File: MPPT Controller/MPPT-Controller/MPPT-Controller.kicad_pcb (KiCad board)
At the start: 4 copper layers, 79 parts, among them J1 Conn_01x02_Pin, J2 Conn_01x02_Pin, J3 Conn_01x02_Pin, J4 Conn_01x02_Pin, J5 USB_C_Receptacle_USB2.0_16P, J6 Conn_01x02_Pin, Q1 IRL540N, SW1 SW_SPDT, U1 ADS1115IDGS, U2 ESP32-WROOM-32D, U3 CH340C, U4 LM1117DT-3.3, U5 LM2596S-ADJ, U6 TC4422, U7 ADS1115IDGS

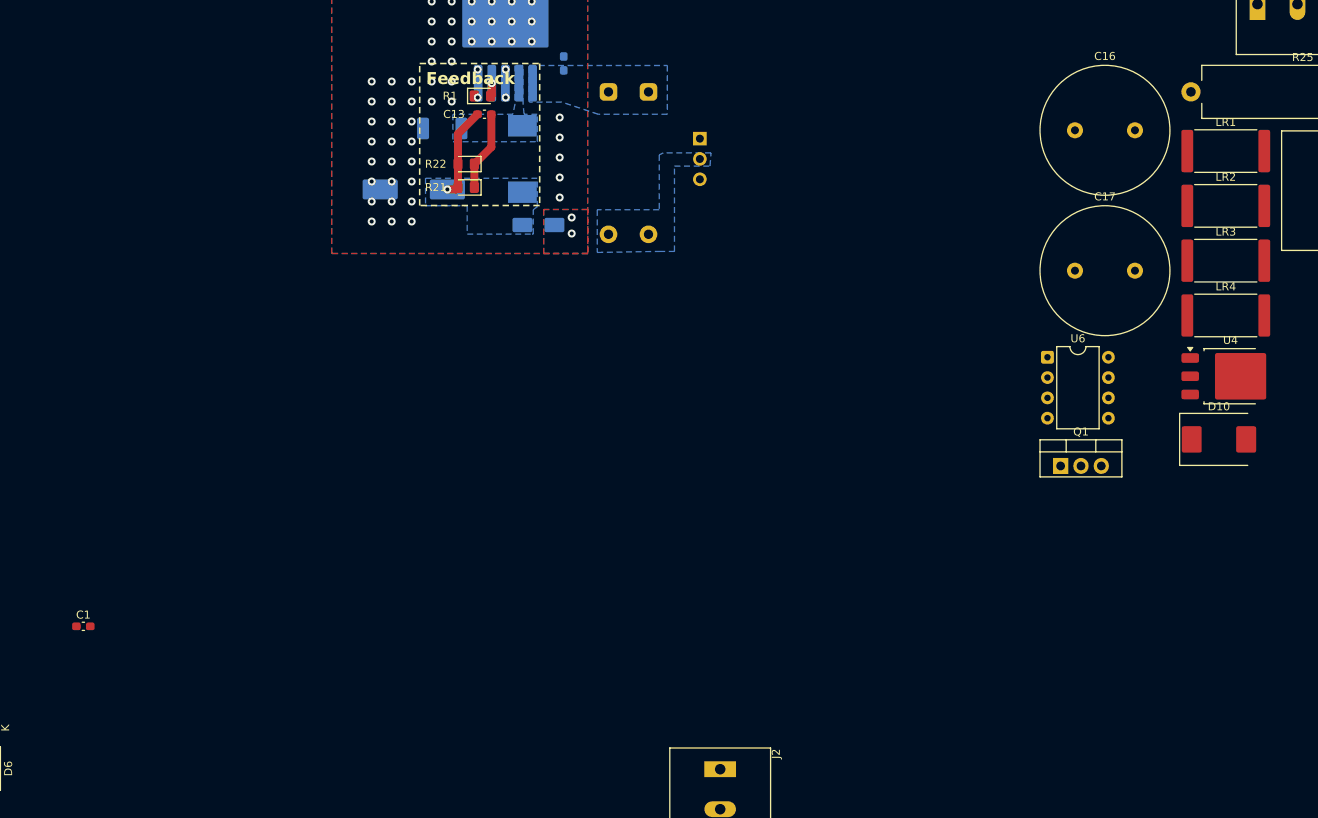
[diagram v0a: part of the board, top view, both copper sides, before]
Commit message: Move Shunts
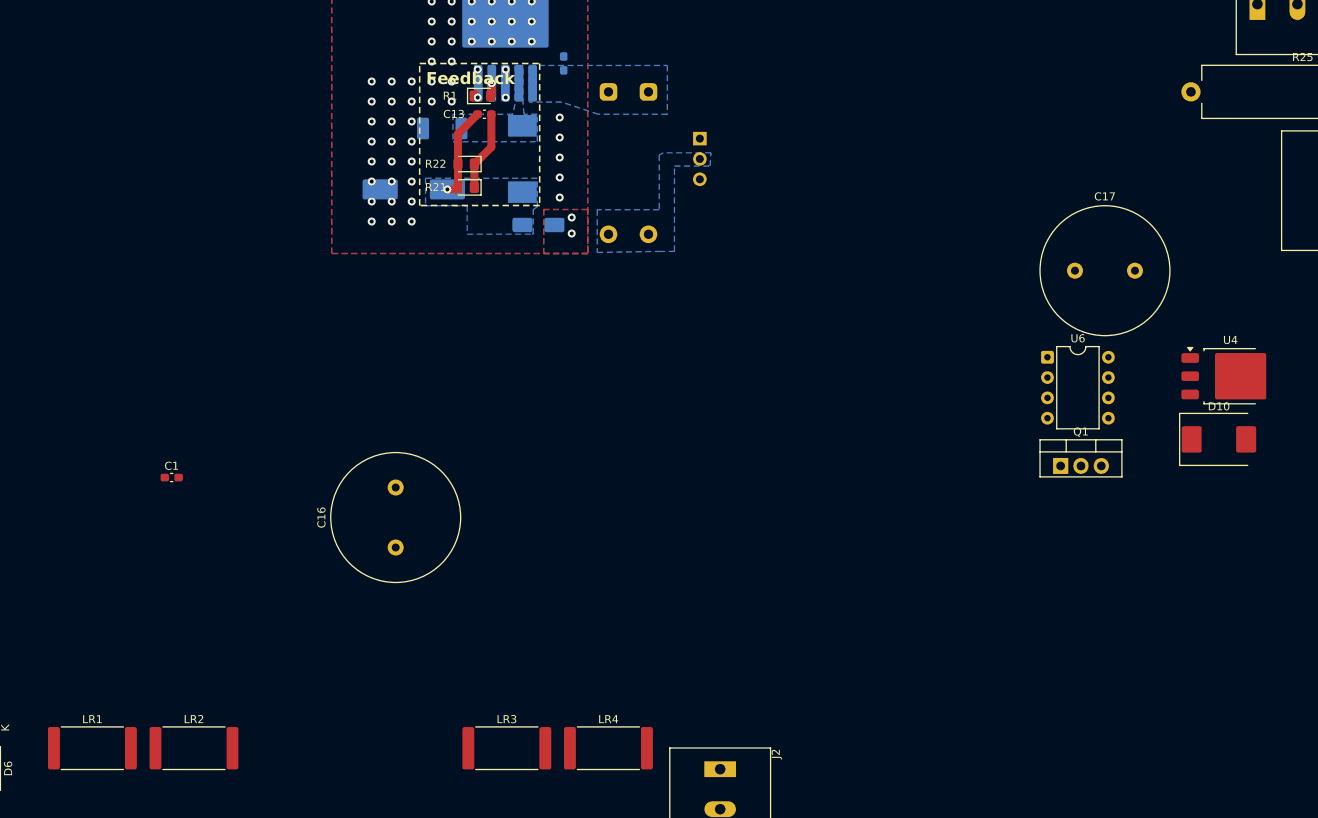
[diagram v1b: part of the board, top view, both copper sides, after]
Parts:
- moved LR1 160.1 mm to (84.1, 116.8)
- moved LR2 145.7 mm to (96.8, 116.8)
- moved LR3 108.6 mm to (135.9, 116.8)
- moved C16 99.6 mm to (122.0, 91.8), turned to 90 degrees
- moved LR4 94.2 mm to (148.6, 116.8)
- moved C1 21.6 mm to (94.0, 83.0)
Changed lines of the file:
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@@
 	(footprint "Capacitor_THT:C_Radial_D16.0mm_H25.0mm_P7.50mm"
 		(layer "F.Cu")
-		(at 206.91 39.595)
+		(at 122 91.75 90)
 		(descr "C, Radial series, Radial, pin pitch=7.50mm, diameter=16mm, height=25mm, Non-Polar Electrolytic Capacitor")
 		(tags "C Radial series Radial pin pitch 7.50mm diameter 16mm height 25mm Non-Polar Electrolytic Capacitor")
 		(property "Reference" "C16"
-			(at 3.75 -9.25 0)
+			(at 3.75 -9.25 90)
 			(layer "F.SilkS")
 			(effects
@@
 		)
 		(property "Value" "470u"
-			(at 3.75 9.25 0)
+			(at 3.75 9.25 90)
 			(layer "F.Fab")
 			(effects
@@
 		)
 		(property "Datasheet" ""
-			(at 0 0 0)
+			(at 0 0 90)
 			(layer "F.Fab")
 			(hide yes)
@@
 		)
 		(property "Description" "Unpolarized capacitor"
-			(at 0 0 0)
+			(at 0 0 90)
 			(layer "F.Fab")
 			(hide yes)
@@
 		)
 		(fp_text user "${REFERENCE}"
-			(at 3.75 0 0)
+			(at 3.75 0 90)
 			(layer "F.Fab")
 			(effects
@@
 		)
 		(pad "1" thru_hole circle
-			(at 0 0)
+			(at 0 0 90)
 			(size 2 2)
 			(drill 1)
@@
 		)
 		(pad "2" thru_hole circle
-			(at 7.5 0)
+			(at 7.5 0 90)
 			(size 2 2)
 			(drill 1)
@@
 	(footprint "Resistor_SMD:R_4020_10251Metric"
 		(layer "F.Cu")
-		(at 225.76 55.895)
+		(at 135.89 116.84)
 		(descr "Resistor SMD 4020 (10251 Metric), square (rectangular) end terminal, IPC-7351 nominal, (Body size source: http://datasheet.octopart.com/HVC0603T5004FET-Ohmite-datasheet-26699797.pdf), generated with kicad-footprint-generator")
 		(tags "resistor")
@@
 	(footprint "Capacitor_SMD:C_0603_1608Metric_Pad1.08x0.95mm_HandSolder"
 		(layer "F.Cu")
-		(at 82.9575 101.6)
+		(at 94 83)
 		(descr "Capacitor SMD 0603 (1608 Metric), square (rectangular) end terminal, IPC-7351 nominal with elongated pad for handsoldering. (Body size source: IPC-SM-782 page 76, https://www.pcb-3d.com/wordpress/wp-content/uploads/ipc-sm-782a_amendment_1_and_2.pdf), generated with kicad-footprint-generator")
 		(tags "capacitor handsolder")
@@
 	(footprint "Resistor_SMD:R_4020_10251Metric"
 		(layer "F.Cu")
-		(at 225.76 49.045)
+		(at 96.7875 116.84)
 		(descr "Resistor SMD 4020 (10251 Metric), square (rectangular) end terminal, IPC-7351 nominal, (Body size source: http://datasheet.octopart.com/HVC0603T5004FET-Ohmite-datasheet-26699797.pdf), generated with kicad-footprint-generator")
 		(tags "resistor")
@@
 	(footprint "Resistor_SMD:R_4020_10251Metric"
 		(layer "F.Cu")
-		(at 225.76 62.745)
+		(at 148.59 116.84)
 		(descr "Resistor SMD 4020 (10251 Metric), square (rectangular) end terminal, IPC-7351 nominal, (Body size source: http://datasheet.octopart.com/HVC0603T5004FET-Ohmite-datasheet-26699797.pdf), generated with kicad-footprint-generator")
 		(tags "resistor")
@@
 	(footprint "Resistor_SMD:R_4020_10251Metric"
 		(layer "F.Cu")
-		(at 225.76 42.195)
+		(at 84.0875 116.84)
 		(descr "Resistor SMD 4020 (10251 Metric), square (rectangular) end terminal, IPC-7351 nominal, (Body size source: http://datasheet.octopart.com/HVC0603T5004FET-Ohmite-datasheet-26699797.pdf), generated with kicad-footprint-generator")
 		(tags "resistor")

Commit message: Compact
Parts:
- moved U2 254.5 mm to (45.9, 66.7)
- moved L2 154.9 mm to (92.7, 66.0), turned to 90 degrees
- moved C17 135.7 mm to (75.0, 88.9)
- moved U6 134.9 mm to (68.6, 66.0)
- moved Q1 109.9 mm to (95.6, 90.2), turned to -90 degrees
- moved C10 47.4 mm to (279.7, 32.0)
- moved C11 47.4 mm to (210.8, 78.2)
- moved C12 47.4 mm to (215.1, 63.1)
- moved C2 47.4 mm to (210.8, 65.6)
- moved C3 47.4 mm to (210.8, 68.1)
- moved C4 47.4 mm to (210.8, 70.7)
- moved C5 47.4 mm to (210.8, 73.2)
- moved C6 47.4 mm to (210.8, 75.7)
- moved C7 47.4 mm to (279.7, 24.4)
- moved C8 47.4 mm to (279.7, 26.9)
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
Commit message: Capacitors
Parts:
- C16, C17: moved to B.Cu
- moved Q1 22.3 mm to (74.5, 97.5), turned to 180 degrees
- moved C17 19.8 mm to (68.2, 107.5)
- moved C16 18.9 mm to (108.2, 107.5), turned to 180 degrees

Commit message: Layout
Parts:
- added HS1: Heatsink_Pad, Heatsink:Heatsink_AAVID_576802B03900G, B.Cu at (71.5, 92.0)
- added M1: Fan_4pin, Connector:FanPinHeader_1x04_P2.54mm_Vertical, F.Cu at (122.9, 81.0)
- Q1: moved to B.Cu
- moved L2 38.0 mm to (80.4, 102.0)
- moved U6 10.5 mm to (58.2, 64.2)
- moved C16 3.22 mm to (105.0, 107.5)
- moved J2 3.22 mm to (136.5, 105.5)
- moved LR3 3.22 mm to (109.8, 102.9)
- moved LR4 3.22 mm to (122.5, 102.9)
- moved Q1 1.11 mm to (73.5, 96.9)
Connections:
- R1 pad 1: GND -> Net-(U5-FB)
- R1 pad 2: Net-(U5-FB) -> GND

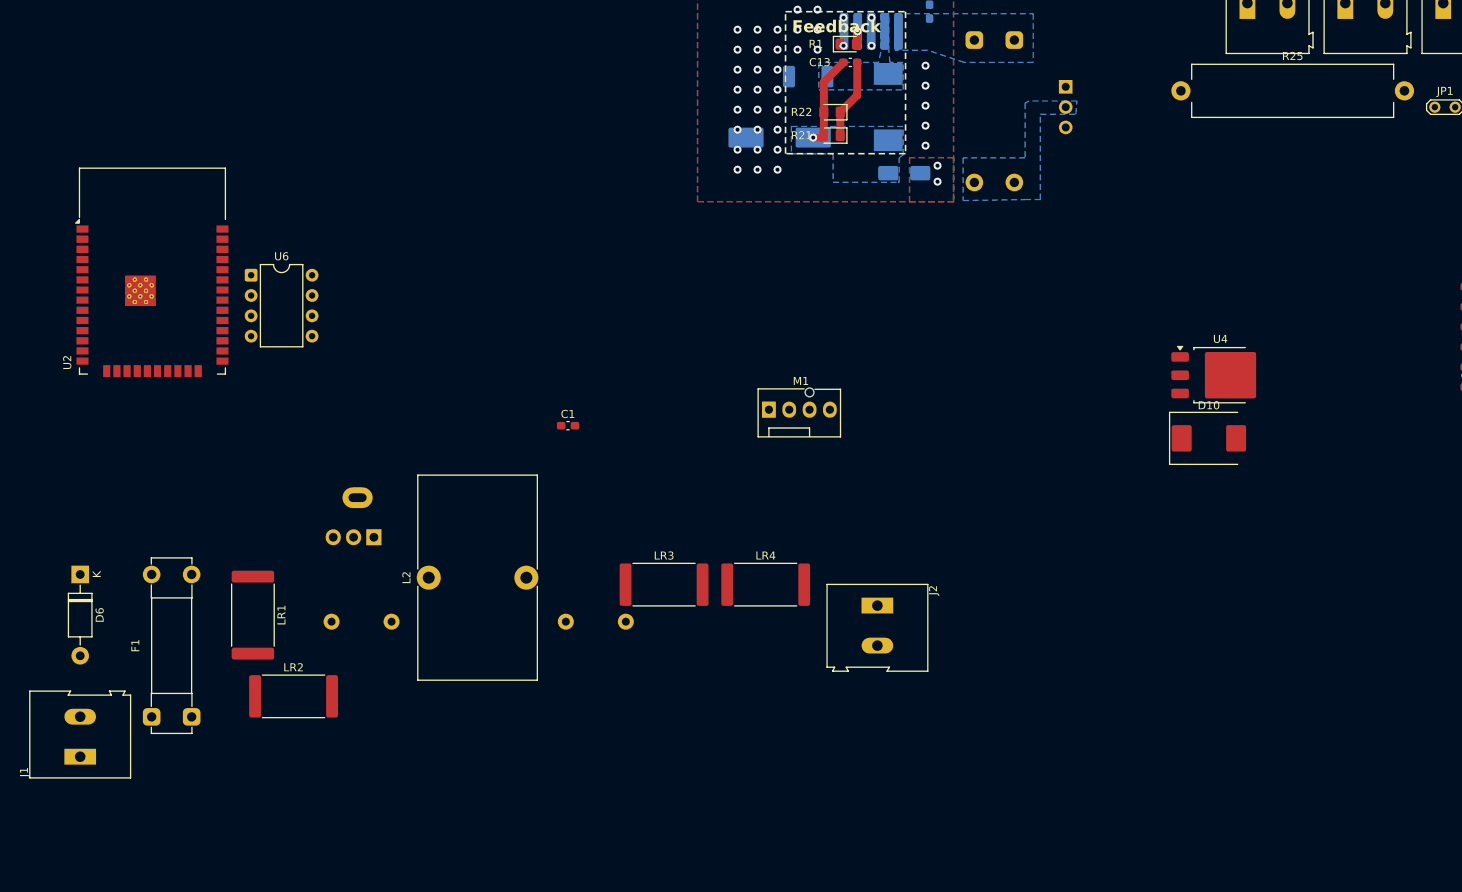
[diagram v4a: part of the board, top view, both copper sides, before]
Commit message: Via Stitching
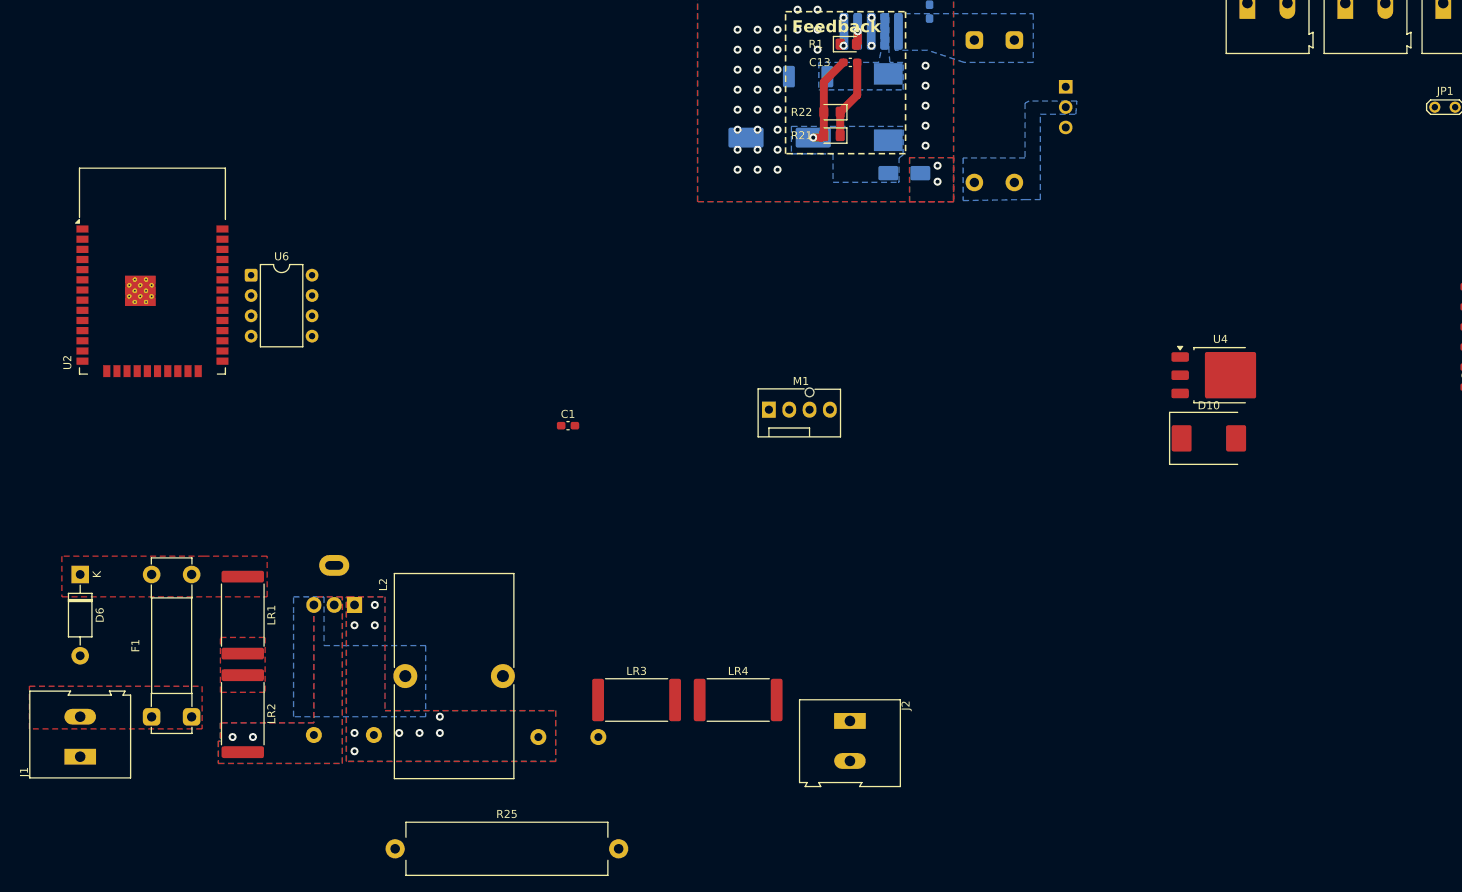
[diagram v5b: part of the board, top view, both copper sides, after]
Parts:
- moved R25 136.5 mm to (76.2, 135.9)
- moved C16 14.8 mm to (101.6, 121.9)
- moved LR3 14.8 mm to (106.4, 117.3)
- moved LR4 14.8 mm to (119.1, 117.3)
- moved J2 14.8 mm to (133.1, 119.9)
- moved C17 14.3 mm to (66.0, 121.7)
- moved L2 12.6 mm to (77.5, 114.3)
- moved HS1 8.95 mm to (68.6, 100.5)
- moved Q1 8.80 mm to (71.1, 105.4)
- moved LR2 6.71 mm to (57.1, 119.0), turned to -90 degrees
- moved LR1 1.27 mm to (57.1, 106.7)
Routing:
- net VinterA: vias 0 -> 2
- net Net-(D10-A): vias 0 -> 9
- added copper zone on B.Cu, net Net-(D10-A)
- added copper zone on F.Cu, net Net-(D10-A)
- added copper zone on B.Cu, net Net-(D10-K)
- added copper zone on F.Cu, net Net-(J1-Pin_2)
- added copper zone on F.Cu, net Net-(LR1-Pad2)
- added copper zone on F.Cu, net Vin
- added copper zone on B.Cu, net VinterA
- added copper zone on F.Cu, net VinterA
